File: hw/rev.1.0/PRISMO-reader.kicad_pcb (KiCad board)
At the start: 2 copper layers, 50 x 51 mm, 49 parts, among them J1 Conn_01x03, J3 PN532 Connector, J4 External 5V power, J5 USB4120-03-C_REVA, K1 G5LE-1, Q1 2N7002, Q2 BC847, Q3 BC847, SW1 Logout button, U1 ESP32-WROOM-32D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

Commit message: Fixed problem with wrong VBUS connection of USB port
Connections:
- J5 pad B4: GND -> +5V
- J5 pad B9: GND -> +5V
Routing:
- net +5V: track 198.8 -> 208.3 mm, vias 12 -> 14
- net GND: track 241.4 -> 237.1 mm

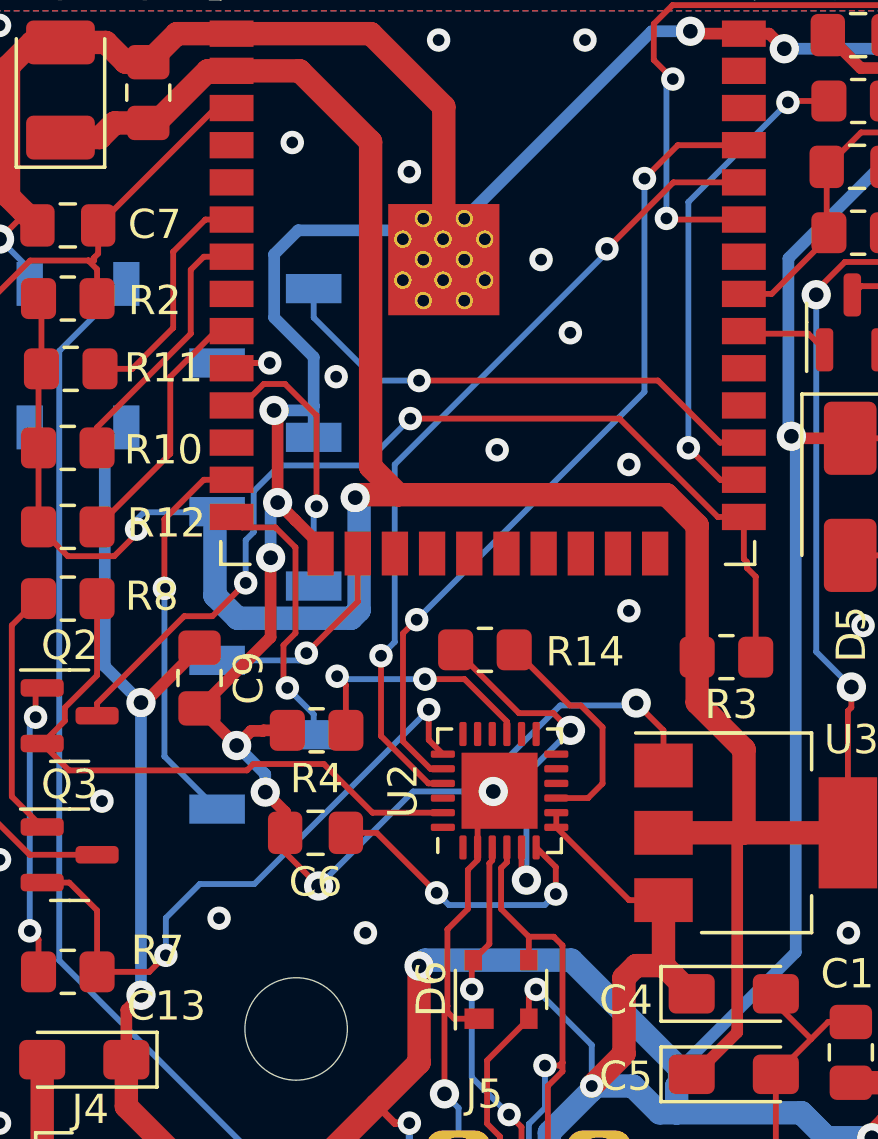
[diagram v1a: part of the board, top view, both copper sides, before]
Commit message: fixed CP2102 peripheral connection
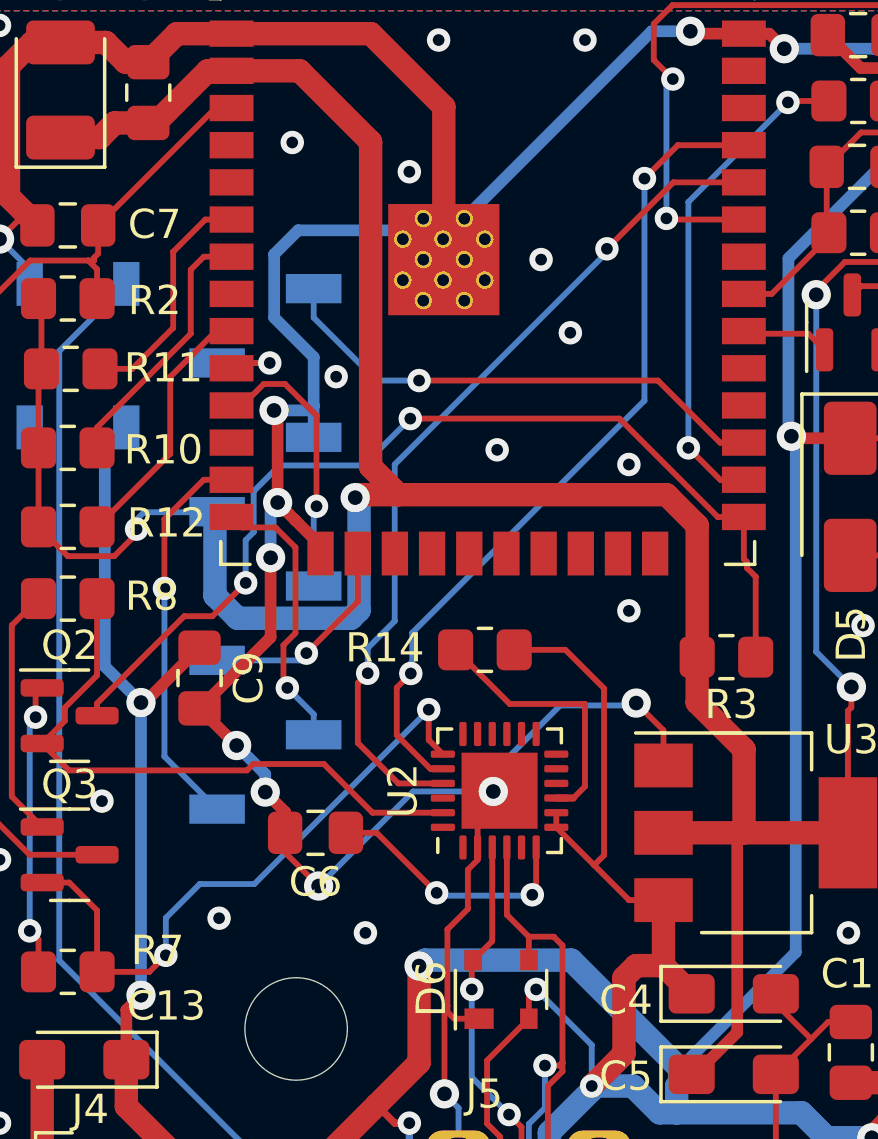
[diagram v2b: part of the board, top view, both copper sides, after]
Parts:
- removed R4: 10k, Resistor_SMD:R_0805_2012Metric_Pad1.20x1.40mm_HandSolder
- R14: value 1k -> 10k
- turned R14 to 180 degrees
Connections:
- R14 pad 1: Net-(U2-VIO) -> +5V
- U2 pad 15: Net-(U2-~{SUSPEND}) -> unconnected-(U2-~{SUSPEND}-Pad15)
- U2 pad 5: Net-(U2-VIO) -> unconnected-(U2-VIO-Pad5)
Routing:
- net Net-(U2-VIO): track 12.4 -> 0.00 mm, vias 2 -> 0
- net +5V: track 208.3 -> 218.1 mm
- net Net-(U2-~{SUSPEND}): track 8.84 -> 0.00 mm, vias 2 -> 0
- net GND: track 237.1 -> 235.2 mm
- net Net-(U2-~{RST}): track 7.82 -> 9.56 mm
- net Net-(U2-VDD): track 10.2 -> 8.94 mm
- net /UART_TX: track 28.2 -> 29.5 mm

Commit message: renamed leds in order of connection
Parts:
- renumbered D3 to D1, D4 to D2, D2 to D3, D1 to D4
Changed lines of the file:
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@@
 	(net 66 "unconnected-(U2-~{WAKEUP}{slash}GPIO.3-Pad11)")
 	(net 67 "unconnected-(U2-RS485{slash}GPIO.2-Pad12)")
-	(net 68 "Net-(D1-DIN)")
-	(net 69 "unconnected-(D1-DOUT-Pad2)")
-	(net 70 "Net-(D2-DIN)")
+	(net 68 "Net-(D1-DOUT)")
+	(net 69 "Net-(D2-DOUT)")
+	(net 70 "unconnected-(D4-DOUT-Pad2)")
 	(net 71 "Net-(D3-DOUT)")
 	(net 72 "unconnected-(U2-VIO-Pad5)")
@@
 		(descr "5.0mm x 5.0mm Addressable RGB LED NeoPixel, https://cdn-shop.adafruit.com/datasheets/WS2812B.pdf")
 		(tags "LED RGB NeoPixel PLCC-4 5050")
-		(property "Reference" "D2"
+		(property "Reference" "D3"
 			(at 0 3.5 180)
 			(layer "B.SilkS")
@@
 			(size 1.5 0.9)
 			(layers "B.Cu" "B.Mask" "B.Paste")
-			(net 68 "Net-(D1-DIN)")
+			(net 71 "Net-(D3-DOUT)")
 			(pinfunction "DOUT")
 			(pintype "output")
@@
 			(size 1.5 0.9)
 			(layers "B.Cu" "B.Mask" "B.Paste")
-			(net 70 "Net-(D2-DIN)")
+			(net 69 "Net-(D2-DOUT)")
 			(pinfunction "DIN")
 			(pintype "input")
@@
 		(descr "5.0mm x 5.0mm Addressable RGB LED NeoPixel, https://cdn-shop.adafruit.com/datasheets/WS2812B.pdf")
 		(tags "LED RGB NeoPixel PLCC-4 5050")
-		(property "Reference" "D1"
+		(property "Reference" "D4"
 			(at 1.382233 3.517767 270)
 			(layer "B.SilkS")
@@
 			(size 1.5 0.9)
 			(layers "B.Cu" "B.Mask" "B.Paste")
-			(net 69 "unconnected-(D1-DOUT-Pad2)")
+			(net 70 "unconnected-(D4-DOUT-Pad2)")
 			(pinfunction "DOUT")
 			(pintype "output+no_connect")
@@
 			(size 1.5 0.9)
 			(layers "B.Cu" "B.Mask" "B.Paste")
-			(net 68 "Net-(D1-DIN)")
+			(net 71 "Net-(D3-DOUT)")
 			(pinfunction "DIN")
 			(pintype "input")
@@
 		(descr "5.0mm x 5.0mm Addressable RGB LED NeoPixel, https://cdn-shop.adafruit.com/datasheets/WS2812B.pdf")
 		(tags "LED RGB NeoPixel PLCC-4 5050")
-		(property "Reference" "D4"
+		(property "Reference" "D2"
 			(at 0 3.5 90)
 			(layer "B.SilkS")
@@
 			(size 1.5 0.9)
 			(layers "B.Cu" "B.Mask" "B.Paste")
-			(net 70 "Net-(D2-DIN)")
+			(net 69 "Net-(D2-DOUT)")
 			(pinfunction "DOUT")
 			(pintype "output")
@@
 			(size 1.5 0.9)
 			(layers "B.Cu" "B.Mask" "B.Paste")
-			(net 71 "Net-(D3-DOUT)")
+			(net 68 "Net-(D1-DOUT)")
 			(pinfunction "DIN")
 			(pintype "input")
@@
 		(descr "5.0mm x 5.0mm Addressable RGB LED NeoPixel, https://cdn-shop.adafruit.com/datasheets/WS2812B.pdf")
 		(tags "LED RGB NeoPixel PLCC-4 5050")
-		(property "Reference" "D3"
+		(property "Reference" "D1"
 			(at 0 3.5 0)
 			(layer "B.SilkS")
@@
 			(size 1.5 0.9)
 			(layers "B.Cu" "B.Mask" "B.Paste")
-			(net 71 "Net-(D3-DOUT)")
+			(net 68 "Net-(D1-DOUT)")
 			(pinfunction "DOUT")
 			(pintype "output")
@@
 	)
 	(segment
-		(start 117.5394 115.941482)
-		(end 129.597918 128)
+		(start 156.532233 85.732233)
+		(end 156.532233 90.632233)
+		(width 0.2)
+		(layer "F.Cu")
+		(net 68)
+	)
+	(segment
+		(start 156.032233 85.032233)
+		(end 156.032233 85.232233)
+		(width 0.2)
+		(layer "F.Cu")
+		(net 68)
+	)
+	(segment
+		(start 156.032233 85.232233)
+		(end 156.532233 85.732233)
+		(width 0.2)
+		(layer "F.Cu")
+		(net 68)
+	)
+	(via
+		(at 156.532233 90.632233)
+		(size 0.8)
+		(drill 0.4)
+		(layers "F.Cu" "B.Cu")
+		(net 68)
+	)
+	(via
+		(at 156.032233 85.032233)
+		(size 0.8)
+		(drill 0.4)
+		(layers "F.Cu" "B.Cu")
+		(net 68)
+	)
+	(segment
+		(start 147.032233 78.582233)
+		(end 148.3 79.85)
 		(width 0.2)
 		(layer "B.Cu")
@@
 	)
 	(segment
-		(start 129.597918 128)
-		(end 144.214466 128)
+		(start 156.532233 90.632233)
+		(end 158.532233 92.632233)
 		(width 0.2)
 		(layer "B.Cu")
@@
 	)
 	(segment
-		(start 117.5394 95.125066)
-		(end 117.5394 115.941482)
+		(start 156.032233 84.132233)
+		(end 156.032233 85.032233)
 		(width 0.2)
 		(layer "B.Cu")
@@
 	)
 	(segment
-		(start 119.832233 92.832233)
-		(end 117.5394 95.125066)
+		(start 148.3 79.85)
+		(end 151.75 79.85)
 		(width 0.2)
 		(layer "B.Cu")
@@
 	)
 	(segment
-		(start 144.214466 128)
-		(end 145.332233 126.882233)
+		(start 158.532233 92.632233)
+		(end 158.532233 93.582233)
+		(width 0.2)
+		(layer "B.Cu")
+		(net 68)
+	)
+	(segment
+		(start 151.75 79.85)
+		(end 156.032233 84.132233)
 		(width 0.2)
 		(layer "B.Cu")
@@
 		(width 0.2)
 		(layer "B.Cu")
-		(net 70)
+		(net 69)
 	)
 	(segment
@@
 		(width 0.2)
 		(layer "B.Cu")
-		(net 70)
+		(net 69)
 	)
 	(segment
@@
 		(width 0.2)
 		(layer "B.Cu")
-		(net 70)
+		(net 69)
 	)
 	(segment
@@
 		(width 0.2)
 		(layer "B.Cu")
-		(net 70)
+		(net 69)
 	)
 	(segment
@@
 		(width 0.2)
 		(layer "B.Cu")
-		(net 70)
+		(net 69)
 	)
 	(segment
@@
 		(width 0.2)
 		(layer "B.Cu")
-		(net 70)
+		(net 69)
 	)
 	(segment
@@
 		(width 0.2)
 		(layer "B.Cu")
-		(net 70)
+		(net 69)
 	)
 	(segment
@@
 		(width 0.2)
 		(layer "B.Cu")
-		(net 70)
+		(net 69)
 	)
 	(segment
@@
 		(width 0.2)
 		(layer "B.Cu")
-		(net 70)
+		(net 69)
 	)
 	(segment
@@
 		(width 0.2)
 		(layer "B.Cu")
-		(net 70)
-	)
-	(segment
-		(start 156.532233 85.732233)
-		(end 156.532233 90.632233)
-		(width 0.2)
-		(layer "F.Cu")
-		(net 71)
-	)
-	(segment
-		(start 156.032233 85.032233)
-		(end 156.032233 85.232233)
-		(width 0.2)
-		(layer "F.Cu")
-		(net 71)
-	)
-	(segment
-		(start 156.032233 85.232233)
-		(end 156.532233 85.732233)
-		(width 0.2)
-		(layer "F.Cu")
-		(net 71)
-	)
-	(via
-		(at 156.532233 90.632233)
-		(size 0.8)
-		(drill 0.4)
-		(layers "F.Cu" "B.Cu")
-		(net 71)
-	)
-	(via
-		(at 156.032233 85.032233)
-		(size 0.8)
-		(drill 0.4)
-		(layers "F.Cu" "B.Cu")
-		(net 71)
-	)
-	(segment
-		(start 147.032233 78.582233)
-		(end 148.3 79.85)
-		(width 0.2)
-		(layer "B.Cu")
-		(net 71)
+		(net 69)
 	)
 	(segment
-		(start 156.532233 90.632233)
-		(end 158.532233 92.632233)
+		(start 117.5394 115.941482)
+		(end 129.597918 128)
 		(width 0.2)
 		(layer "B.Cu")
@@
 	)
 	(segment
-		(start 156.032233 84.132233)
-		(end 156.032233 85.032233)
+		(start 129.597918 128)
+		(end 144.214466 128)
 		(width 0.2)
 		(layer "B.Cu")
@@
 	)
 	(segment
-		(start 148.3 79.85)
-		(end 151.75 79.85)
+		(start 117.5394 95.125066)
+		(end 117.5394 115.941482)
 		(width 0.2)
 		(layer "B.Cu")
@@
 	)
 	(segment
-		(start 158.532233 92.632233)
-		(end 158.532233 93.582233)
+		(start 119.832233 92.832233)
+		(end 117.5394 95.125066)
 		(width 0.2)
 		(layer "B.Cu")
@@
 	)
 	(segment
-		(start 151.75 79.85)
-		(end 156.032233 84.132233)
+		(start 144.214466 128)
+		(end 145.332233 126.882233)
 		(width 0.2)
 		(layer "B.Cu")

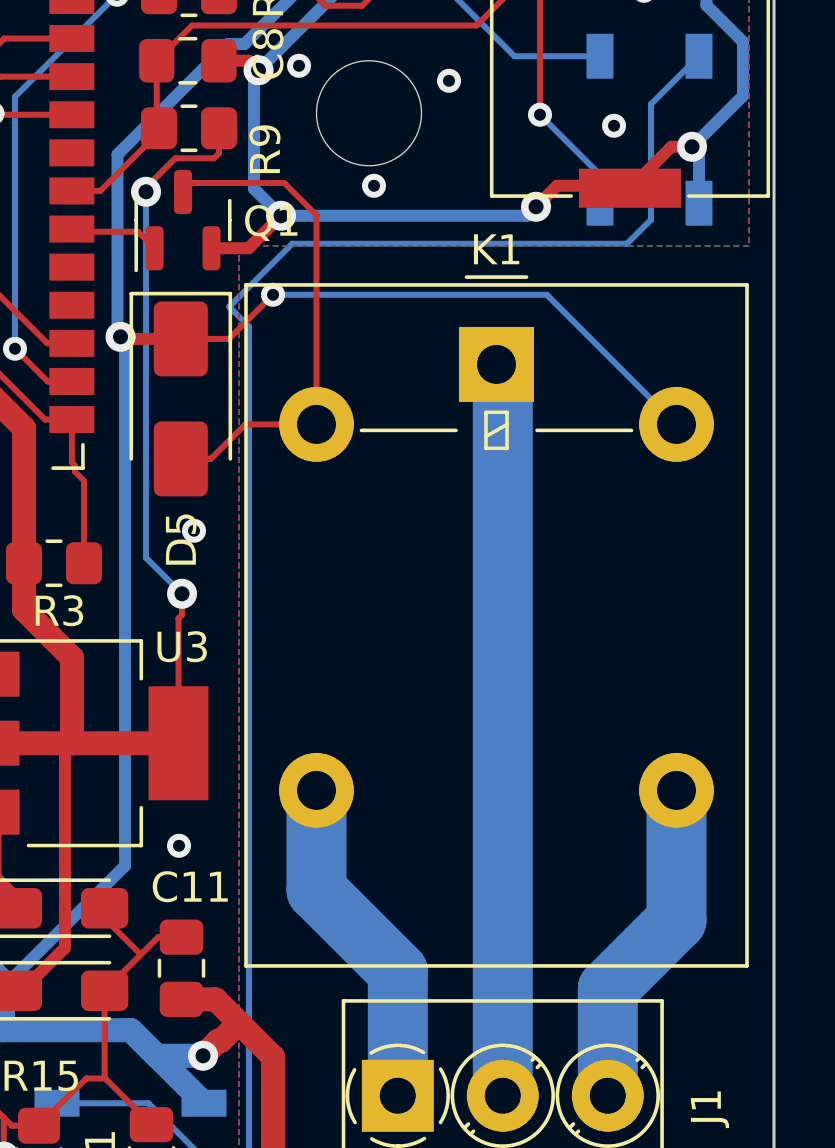
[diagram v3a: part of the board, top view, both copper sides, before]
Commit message: - moved relay position on a few mm - fixed hostname configuration - deleted wifi connection timeout - decreased watchdog period
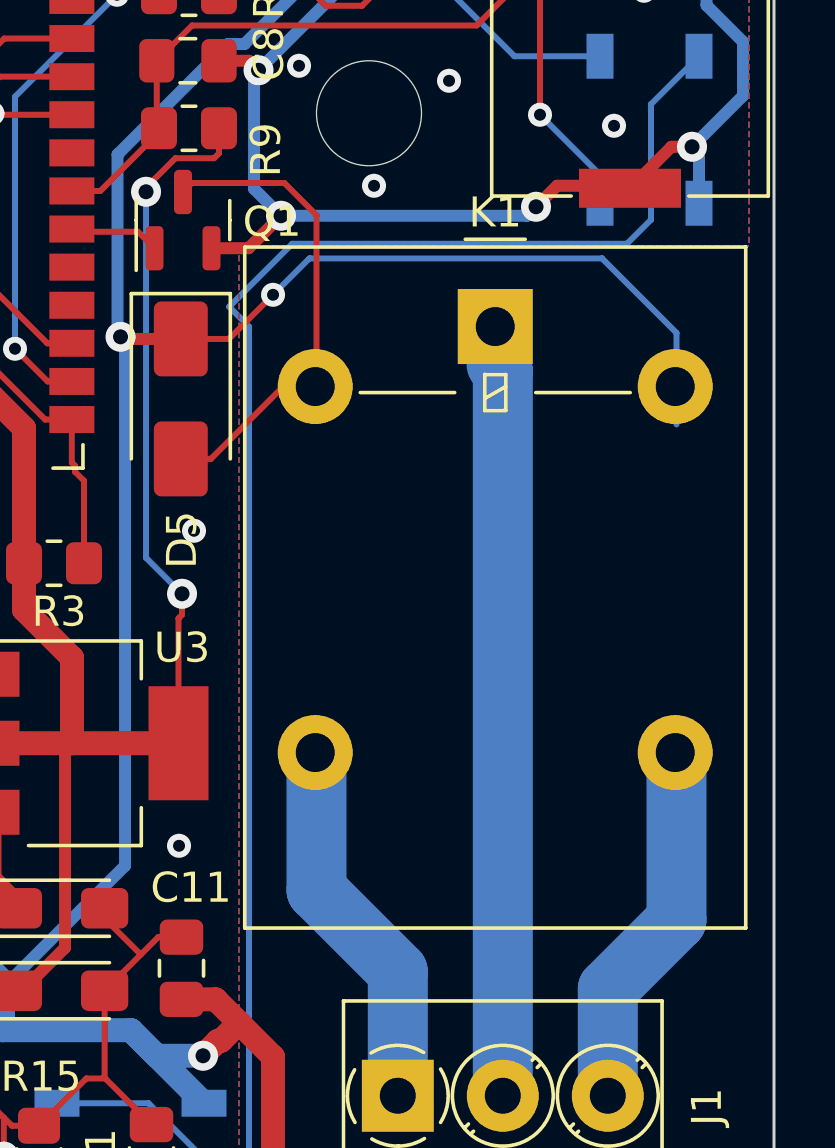
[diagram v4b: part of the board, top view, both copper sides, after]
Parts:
- moved K1 1.26 mm to (155.0, 97.7)
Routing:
- net +5V: track 218.1 -> 220.9 mm
- net Net-(J1-Pin_3): track 11.1 -> 12.4 mm
- net Net-(J1-Pin_1): track 11.3 -> 12.6 mm
- net Net-(D5-A): track 17.0 -> 16.3 mm
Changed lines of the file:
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@@
 			(plot_on_all_layers_selection 0x00000000_00000000_00000000_00000000)
 			(disableapertmacros no)
-			(usegerberextensions no)
-			(usegerberattributes yes)
-			(usegerberadvancedattributes yes)
-			(creategerberjobfile yes)
+			(usegerberextensions yes)
+			(usegerberattributes no)
+			(usegerberadvancedattributes no)
+			(creategerberjobfile no)
 			(dashed_line_dash_ratio 12.000000)
 			(dashed_line_gap_ratio 3.000000)
@@
 			(plot_black_and_white yes)
 			(plotinvisibletext no)
-			(sketchpadsonfab no)
+			(sketchpadsonfab yes)
 			(plotpadnumbers no)
 			(hidednponfab no)
 			(sketchdnponfab yes)
 			(crossoutdnponfab yes)
-			(subtractmaskfromsilk no)
+			(subtractmaskfromsilk yes)
 			(outputformat 1)
 			(mirror no)
@@
 	(footprint "Relay_THT:Relay_SPDT_Omron-G5LE-1"
 		(layer "F.Cu")
-		(at 155.082233 98.954733)
+		(at 155.04 97.6925)
 		(descr "Omron Relay SPDT, http://www.omron.com/ecb/products/pdf/en-g5le.pdf")
 		(tags "Omron Relay SPDT")
@@
 		)
 		(fp_text user "${REFERENCE}"
-			(at 0 8.7 0)
+			(at 0 8.6275 0)
 			(layer "F.Fab")
 			(effects
@@
 	)
 	(segment
+		(start 148.847768 95.42)
+		(end 147.633884 96.633884)
+		(width 0.2)
+		(layer "B.Cu")
+		(net 3)
+	)
+	(segment
 		(start 138.632233 121.147233)
 		(end 138.047233 121.147233)
@@
 	)
 	(segment
-		(start 156.761384 96.633884)
-		(end 147.633884 96.633884)
-		(width 0.2)
-		(layer "B.Cu")
-		(net 3)
-	)
-	(segment
 		(start 142.45 91.956497)
 		(end 142.45 97.934832)
@@
 	)
 	(segment
+		(start 158.6 95.42)
+		(end 148.847768 95.42)
+		(width 0.2)
+		(layer "B.Cu")
+		(net 3)
+	)
+	(segment
+		(start 161.082233 100.954733)
+		(end 161.082233 97.902233)
+		(width 0.2)
+		(layer "B.Cu")
+		(net 3)
+	)
+	(segment
 		(start 119.096092 98.468374)
 		(end 119.096092 105.896092)
@@
 	)
 	(segment
-		(start 161.082233 100.954733)
-		(end 156.761384 96.633884)
-		(width 0.2)
-		(layer "B.Cu")
-		(net 3)
-	)
-	(segment
 		(start 142.45 97.934832)
 		(end 142.55 98.034832)
@@
 	)
 	(segment
+		(start 161.082233 97.902233)
+		(end 158.6 95.42)
+		(width 0.2)
+		(layer "B.Cu")
+		(net 3)
+	)
+	(segment
 		(start 135.732233 120.232233)
 		(end 135.732233 120.370887)
@@
 	)
 	(segment
-		(start 144.932232 92.907234)
-		(end 148.009316 92.907234)
+		(start 148.009316 92.907234)
+		(end 144.932232 92.907234)
 		(width 0.2)
 		(layer "F.Cu")
@@
 	)
 	(segment
-		(start 145.559733 102.104733)
-		(end 146.709733 100.954733)
+		(start 144.559733 102.104733)
+		(end 145.559733 102.104733)
 		(width 0.2)
 		(layer "F.Cu")
@@
 	)
 	(segment
-		(start 144.559733 102.104733)
-		(end 145.559733 102.104733)
+		(start 144.932232 92.907234)
+		(end 144.632233 93.207233)
 		(width 0.2)
 		(layer "F.Cu")
@@
 	)
 	(segment
-		(start 144.632233 93.207233)
-		(end 144.932232 92.907234)
+		(start 145.559733 102.104733)
+		(end 147.971966 99.6925)
 		(width 0.2)
 		(layer "F.Cu")
@@
 	)
 	(segment
-		(start 149.082233 93.980151)
-		(end 149.082233 100.954733)
+		(start 147.971966 99.6925)
+		(end 149.082233 99.6925)
 		(width 0.2)
 		(layer "F.Cu")
@@
 	)
 	(segment
-		(start 146.709733 100.954733)
-		(end 149.082233 100.954733)
+		(start 149.082233 93.980151)
+		(end 148.009316 92.907234)
 		(width 0.2)
 		(layer "F.Cu")
@@
 	)
 	(segment
-		(start 148.009316 92.907234)
+		(start 149.082233 99.6925)
 		(end 149.082233 93.980151)
 		(width 0.2)
@@
 	)
 	(segment
-		(start 151.792233 123.332233)
-		(end 151.792233 119.192233)
+		(start 149.082233 111.934733)
+		(end 149.04 111.8925)
+		(width 2)
+		(layer "B.Cu")
+		(net 13)
+	)
+	(segment
+		(start 151.792233 119.192233)
+		(end 149.082233 116.482233)
 		(width 2)
 		(layer "B.Cu")
@@
 	(segment
 		(start 149.082233 116.482233)
-		(end 149.082233 113.154733)
+		(end 149.082233 111.934733)
 		(width 2)
 		(layer "B.Cu")
@@
 	)
 	(segment
-		(start 151.792233 119.192233)
-		(end 149.082233 116.482233)
+		(start 151.792233 123.332233)
+		(end 151.792233 119.192233)
 		(width 2)
 		(layer "B.Cu")
@@
 	)
 	(segment
-		(start 158.792233 119.772233)
-		(end 161.082233 117.482233)
+		(start 161.082233 117.482233)
+		(end 161.082233 111.934733)
 		(width 2)
 		(layer "B.Cu")
@@
 	)
 	(segment
-		(start 161.082233 117.482233)
-		(end 161.082233 113.154733)
+		(start 158.792233 119.772233)
+		(end 161.082233 117.482233)
 		(width 2)
 		(layer "B.Cu")
@@
 		(width 2)
 		(layer "B.Cu")
+		(net 14)
+	)
+	(segment
+		(start 161.082233 111.934733)
+		(end 161.04 111.8925)
+		(width 2)
+		(layer "B.Cu")
